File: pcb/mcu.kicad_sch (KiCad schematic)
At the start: 29 parts, among them J1 SWD+UART, SW1 BOOT, SW2 RESET, SW3 USER, U1 RP2350A, U2 W25Q128JVS, Y1 12MHz

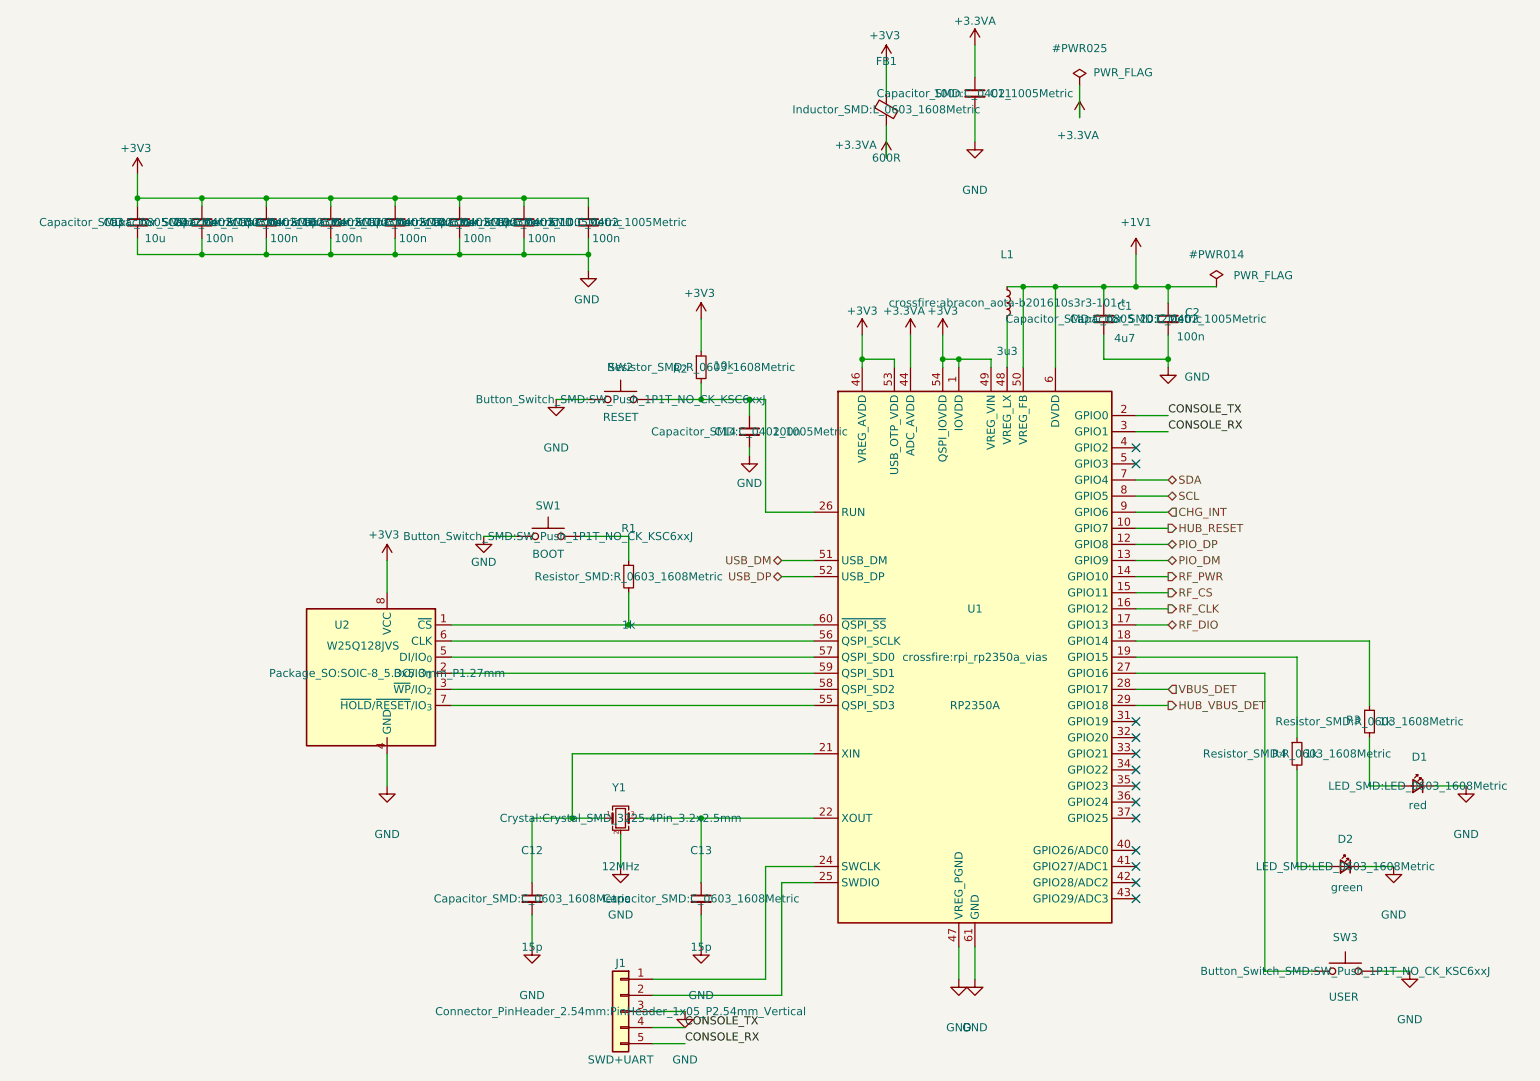
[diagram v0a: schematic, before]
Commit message: checkpoint the battery, PD and radio design as it stood
The last state of the full-featured board before it is reduced to a single
USB-C input: the power block re-placed part by part in order of importance,
the charger's signal pins fanned out, the differential pairs renamed so the
layout tool recognises them, the 3.3 V converter's feedback divider joined
to its pin, the FETs given their part number, and the non-printing fields
hidden on the schematic. The layout is incomplete and is recorded as such.

Co-Authored-By: Claude Fable 5.1 <noreply@anthropic.com>
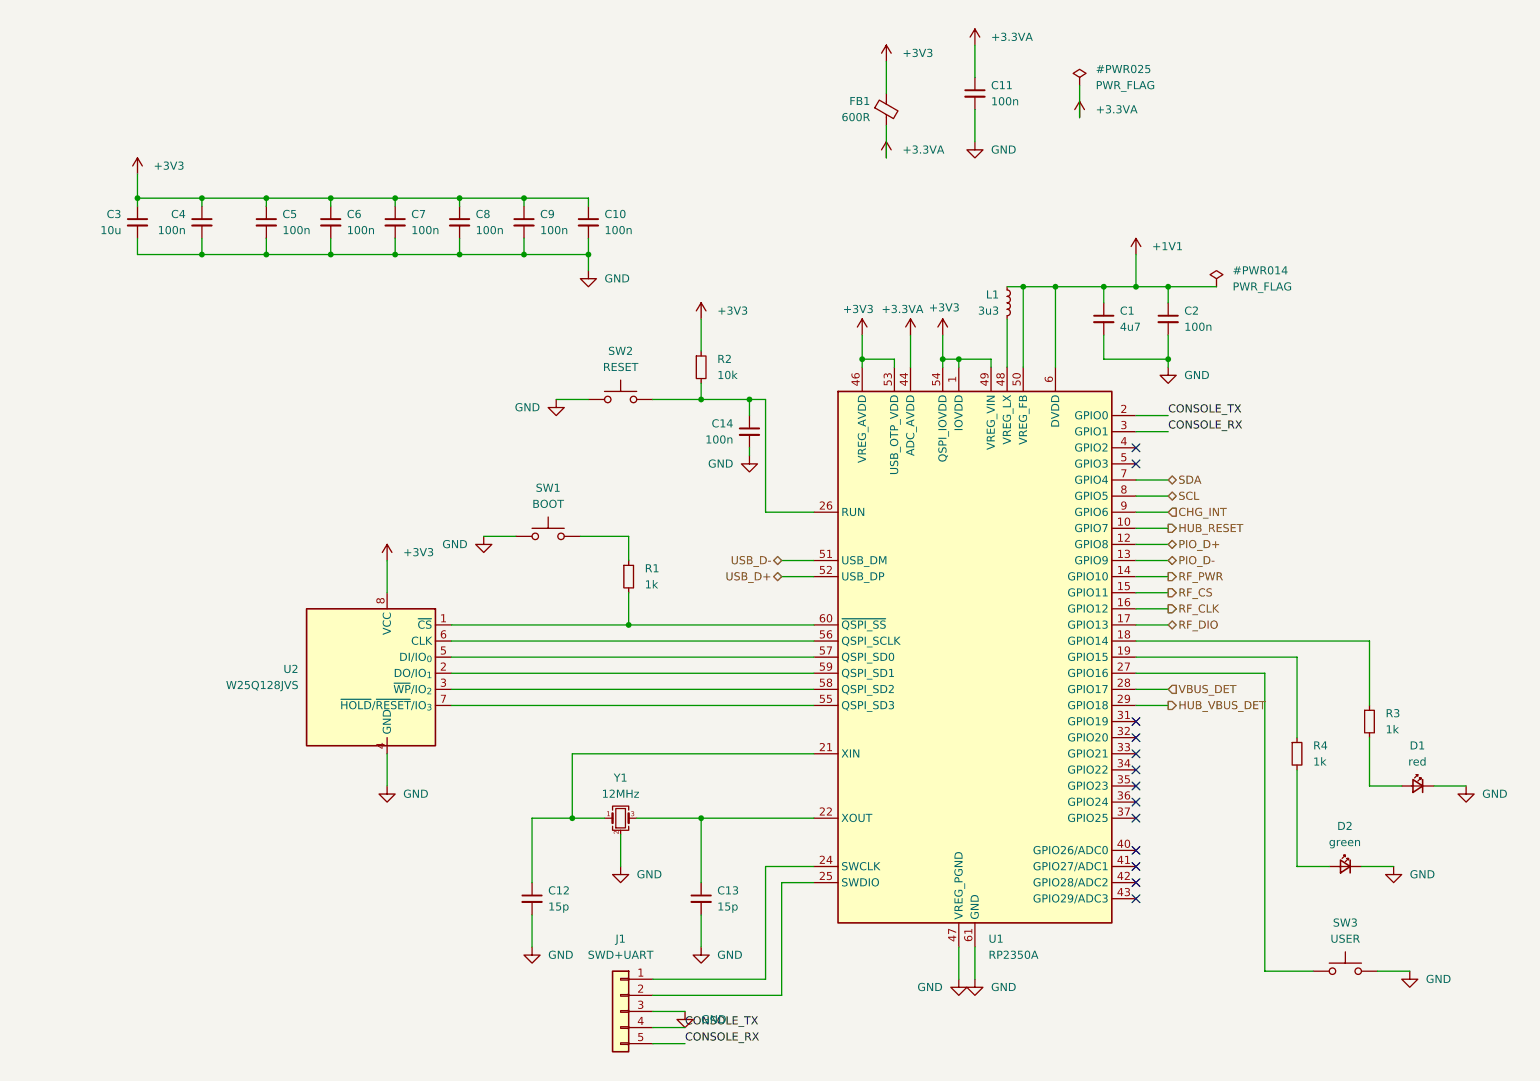
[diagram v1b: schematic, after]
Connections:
- net PIO_DM renamed PIO_D-
- net PIO_DP renamed PIO_D+
- net USB_DM renamed USB_D-
- net USB_DP renamed USB_D+

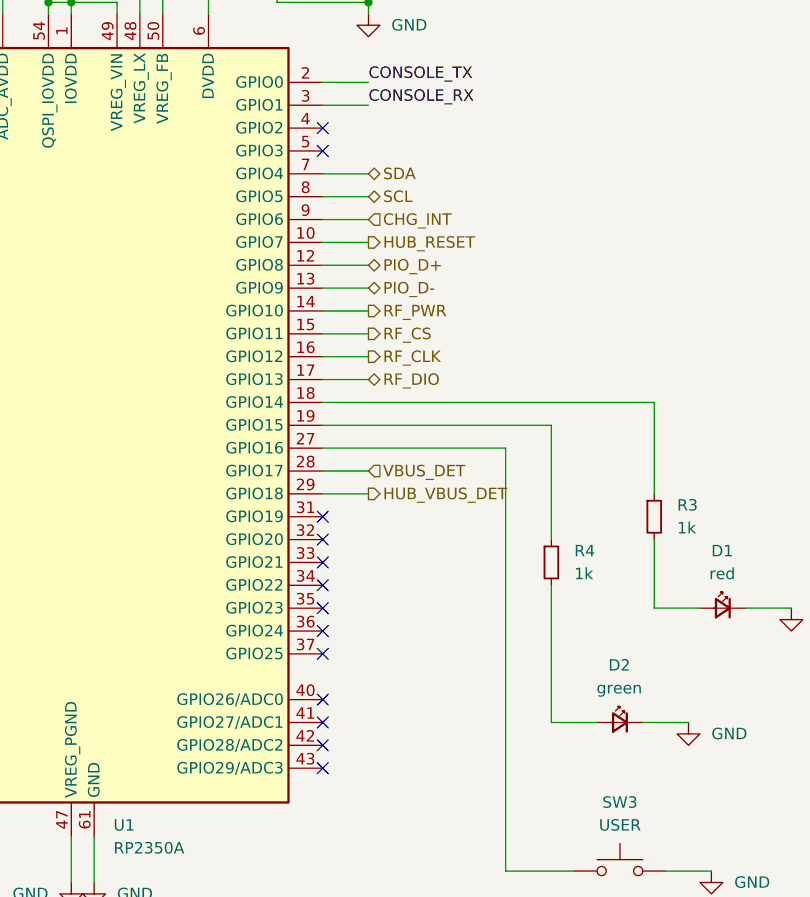
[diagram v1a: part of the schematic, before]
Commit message: reduce the board to a single USB-C input
The PD sink and its connector, the charger and the cell, the input and ship
switches, the 5 V boost, the 3.3 V buck-boost and the radio come off. The
one remaining USB-C receptacle carries data to the hardware controller and
its VBUS is the 5 V rail: straight to the four port switches, and to a
fixed 3.3 V buck (AP63203) for everything else.

The two CC pins are read by ADC inputs through 10k into 100n, in series so
the 5.1k termination is not loaded, so firmware can tell a 3 A source from
a 1.5 A one from a default port and power the ports to fit.

Schematic: radio and upstream_power sheets removed, power sheet redrawn,
seven MCU pins freed and two taken. Board: 61 footprints and 514 tracks and
vias removed, survivors re-netted from the netlist, new parts loaded but
not placed. The layout is to be redone and the design document says so; it
is rewritten for this design, with what the single input gives up stated.

Co-Authored-By: Claude Fable 5.1 <noreply@anthropic.com>
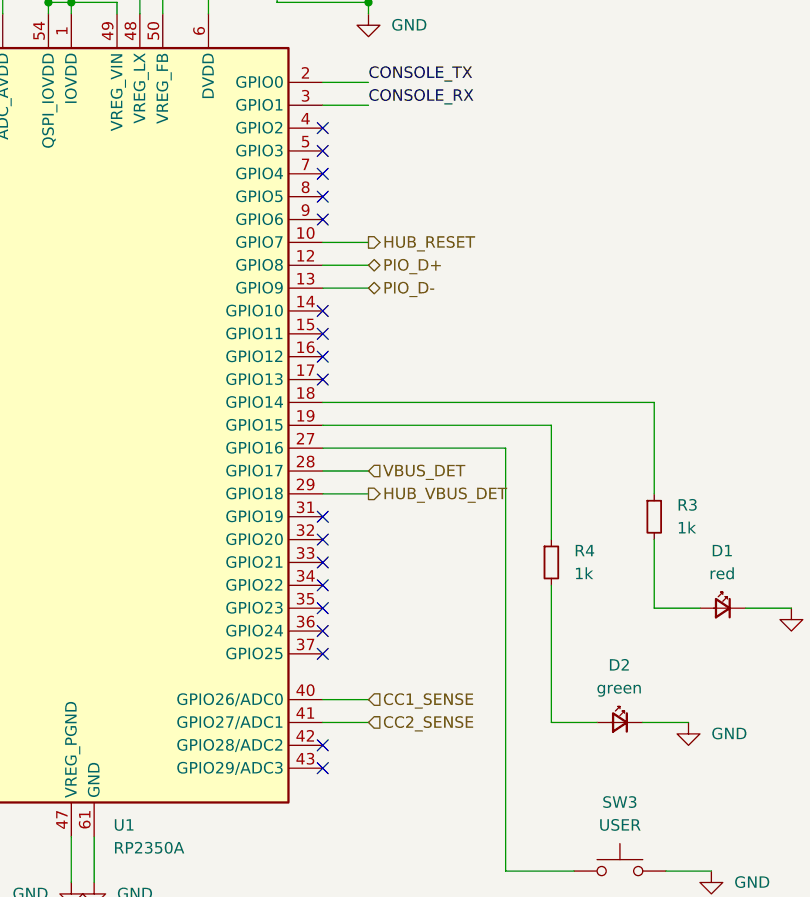
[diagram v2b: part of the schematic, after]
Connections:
- net CC1_SENSE: now reaches U1.40 (GPIO26/ADC0)
- net CC2_SENSE: now reaches U1.41 (GPIO27/ADC1)
- net CHG_INT: no longer names the net of U1.9 (GPIO6)
- net RF_CLK: no longer names the net of U1.16 (GPIO12)
- net RF_CS: no longer names the net of U1.15 (GPIO11)
- net RF_DIO: no longer names the net of U1.17 (GPIO13)
- net RF_PWR: no longer names the net of U1.14 (GPIO10)
- net SCL: no longer names the net of U1.8 (GPIO5)
- net SDA: no longer names the net of U1.7 (GPIO4)
- no-connect marks 13 -> 18
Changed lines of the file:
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@@
 	)
 	(no_connect
-		(at 228.6 172.72)
-	)
-	(no_connect
 		(at 228.6 165.1)
 	)
@@
 	)
 	(no_connect
-		(at 228.6 170.18)
-	)
-	(no_connect
 		(at 228.6 106.68)
 	)
@@
 	(wire
 		(pts
-			(xy 228.6 111.76) (xy 233.68 111.76)
-		)
-		(stroke
-			(width 0)
-			(type solid)
-		)
-	)
-	(wire
-		(pts
-			(xy 228.6 127) (xy 233.68 127)
-		)
-		(stroke
-			(width 0)
-			(type solid)
-		)
-	)
-	(wire
-		(pts
 			(xy 200.66 93.98) (xy 200.66 92.71)
 		)
@@
 	(wire
 		(pts
-			(xy 228.6 132.08) (xy 233.68 132.08)
-		)
-		(stroke
-			(width 0)
-			(type solid)
-		)
-	)
-	(wire
-		(pts
 			(xy 228.6 101.6) (xy 233.68 101.6)
 		)
@@
 	(wire
 		(pts
-			(xy 228.6 129.54) (xy 233.68 129.54)
-		)
-		(stroke
-			(width 0)
-			(type solid)
-		)
-	)
-	(wire
-		(pts
 			(xy 266.7 189.23) (xy 271.78 189.23)
 		)
@@
 	(wire
 		(pts
-			(xy 228.6 114.3) (xy 233.68 114.3)
-		)
-		(stroke
-			(width 0)
-			(type solid)
-		)
-	)
-	(wire
-		(pts
 			(xy 200.66 185.42) (xy 200.66 190.5)
 		)
@@
 	(wire
 		(pts
-			(xy 228.6 134.62) (xy 233.68 134.62)
-		)
-		(stroke
-			(width 0)
-			(type solid)
-		)
-	)
-	(wire
-		(pts
 			(xy 228.6 119.38) (xy 233.68 119.38)
 		)
@@
 	(wire
 		(pts
-			(xy 228.6 116.84) (xy 233.68 116.84)
-		)
-		(stroke
-			(width 0)
-			(type solid)
-		)
-	)
-	(wire
-		(pts
 			(xy 120.65 134.62) (xy 177.8 134.62)
 		)
@@
 		)
 	)
-	(hierarchical_label "SCL"
-		(shape bidirectional)
-		(at 233.68 114.3 0)
-		(effects
-			(font
-				(size 1.27 1.27)
-			)
-			(justify left)
-		)
-	)
 	(hierarchical_label "HUB_RESET"
 		(shape output)
@@
 		)
 	)
-	(hierarchical_label "RF_CLK"
-		(shape output)
-		(at 233.68 132.08 0)
-		(effects
-			(font
-				(size 1.27 1.27)
-			)
-			(justify left)
-		)
-	)
-	(hierarchical_label "SDA"
-		(shape bidirectional)
-		(at 233.68 111.76 0)
-		(effects
-			(font
-				(size 1.27 1.27)
-			)
-			(justify left)
-		)
-	)
-	(hierarchical_label "RF_CS"
-		(shape output)
-		(at 233.68 129.54 0)
-		(effects
-			(font
-				(size 1.27 1.27)
-			)
-			(justify left)
-		)
-	)
 	(hierarchical_label "PIO_D-"
 		(shape bidirectional)
@@
 		)
 	)
-	(hierarchical_label "RF_DIO"
-		(shape bidirectional)
-		(at 233.68 134.62 0)
-		(effects
-			(font
-				(size 1.27 1.27)
-			)
-			(justify left)
-		)
-	)
-	(hierarchical_label "RF_PWR"
-		(shape output)
-		(at 233.68 127 0)
-		(effects
-			(font
-				(size 1.27 1.27)
-			)
-			(justify left)
-		)
-	)
 	(hierarchical_label "USB_D+"
 		(shape bidirectional)
@@
 		)
 	)
-	(hierarchical_label "CHG_INT"
-		(shape input)
-		(at 233.68 116.84 0)
-		(effects
-			(font
-				(size 1.27 1.27)
-			)
-			(justify left)
-		)
-	)
 	(hierarchical_label "PIO_D+"
 		(shape bidirectional)
@@
 		)
 	)
+	(no_connect
+		(at 228.6 111.76)
+	)
+	(no_connect
+		(at 228.6 114.3)
+	)
+	(no_connect
+		(at 228.6 116.84)
+	)
+	(no_connect
+		(at 228.6 132.08)
+	)
+	(no_connect
+		(at 228.6 129.54)
+	)
+	(no_connect
+		(at 228.6 134.62)
+	)
+	(no_connect
+		(at 228.6 127)
+	)
+	(wire
+		(pts
+			(xy 228.6 170.18) (xy 233.68 170.18)
+		)
+		(stroke
+			(width 0)
+			(type default)
+		)
+	)
+	(hierarchical_label "CC1_SENSE"
+		(shape input)
+		(at 233.68 170.18 0)
+		(effects
+			(font
+				(size 1.27 1.27)
+			)
+			(justify left)
+		)
+	)
+	(wire
+		(pts
+			(xy 228.6 172.72) (xy 233.68 172.72)
+		)
+		(stroke
+			(width 0)
+			(type default)
+		)
+	)
+	(hierarchical_label "CC2_SENSE"
+		(shape input)
+		(at 233.68 172.72 0)
+		(effects
+			(font
+				(size 1.27 1.27)
+			)
+			(justify left)
+		)
+	)

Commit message: resistors to 0402
All nineteen, on the schematic and on the board, each keeping its identity,
position, face and nets; the placement is then rebuilt so the smaller parts
settle where they fit. The indicators stay 0603. Rules check clean; 39
items open, eighteen of them the pairs.

Co-Authored-By: Claude Fable 5.1 <noreply@anthropic.com>
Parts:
- R1, R2, R3, R4: footprint Resistor_SMD:R_0603_1608Metric -> Resistor_SMD:R_0402_1005Metric
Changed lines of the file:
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@@
 			)
 		)
-		(property "Footprint" "Resistor_SMD:R_0603_1608Metric"
+		(property "Footprint" "Resistor_SMD:R_0402_1005Metric"
 			(at 254 154.94 0)
 			(hide yes)
@@
 			)
 		)
-		(property "Footprint" "Resistor_SMD:R_0603_1608Metric"
+		(property "Footprint" "Resistor_SMD:R_0402_1005Metric"
 			(at 148.59 127 0)
 			(hide yes)
@@
 			)
 		)
-		(property "Footprint" "Resistor_SMD:R_0603_1608Metric"
+		(property "Footprint" "Resistor_SMD:R_0402_1005Metric"
 			(at 265.43 149.86 0)
 			(hide yes)
@@
 			)
 		)
-		(property "Footprint" "Resistor_SMD:R_0603_1608Metric"
+		(property "Footprint" "Resistor_SMD:R_0402_1005Metric"
 			(at 160.02 93.98 0)
 			(hide yes)

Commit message: hand layout and routing of the single-input board
All six pairs routed, the port power and fault lines moved to the back,
the crystal above the processor, a 100 nF on DVDD pin 23 added to the
schematic as C15. Rules check: three shorts on HUB_RESET's back-layer run
and three clearances still to clear; thirteen connections still open.

Co-Authored-By: Claude Fable 5.1 <noreply@anthropic.com>
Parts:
- added C15: 100n, Capacitor_SMD:C_0402_1005Metric, symbol Device:C_Small
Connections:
- net +1V1: now also C15.1
- net GND: now also C15.2

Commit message: take the processor's regulator parts from the vendor's reference design
4.7 uF in 0402 on VREG_VIN and on the core rail, where this board had 10 uF
and 4.7 uF in 0805, and a 33 ohm / 4.7 uF filter on VREG_AVDD, which it
did not have at all. The crystal's load capacitors go to 0402 and the
3.3 V buck's capacitors to 0603. Footprints are swapped on the board in
place so the layout stands; R5 and C16 are parked outside the left edge.

Co-Authored-By: Claude Fable 5.1 <noreply@anthropic.com>
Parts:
- added C16: 4u7, Capacitor_SMD:C_0402_1005Metric, symbol Device:C_Small
- added R5: 33R, Resistor_SMD:R_0402_1005Metric, symbol Device:R_Small
- C1: footprint Capacitor_SMD:C_0805_2012Metric -> Capacitor_SMD:C_0402_1005Metric; Dielectric X7R -> X5R; Voltage 16V -> 6.3V
- C12, C13: footprint Capacitor_SMD:C_0603_1608Metric -> Capacitor_SMD:C_0402_1005Metric
- C3: value 10u -> 4u7; footprint Capacitor_SMD:C_0805_2012Metric -> Capacitor_SMD:C_0402_1005Metric; Dielectric X7R -> X5R; Voltage 16V -> 6.3V
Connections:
- net +3V3: now also R5.1; no longer U1.46 (VREG_AVDD)
- net GND: now also C16.2
- new net: C16.1, R5.2, U1.46 (VREG_AVDD)

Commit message: the analogue-supply filter as 100 ohms and 1 uF: the same corner, a smaller part, no 4 V rating
Co-Authored-By: Claude Fable 5.1 <noreply@anthropic.com>
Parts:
- C16: value 4u7 -> 1u
- R5: value 33R -> 100R
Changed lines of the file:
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@@
 			)
 		)
-		(property "Value" "33R"
+		(property "Value" "100R"
 			(at 187.96 90.17 0)
 			(show_name no)
@@
 			)
 		)
-		(property "Value" "4u7"
+		(property "Value" "1u"
 			(at 176.53 95.25 0)
 			(show_name no)
